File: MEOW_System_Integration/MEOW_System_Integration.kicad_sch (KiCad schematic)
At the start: 1 part

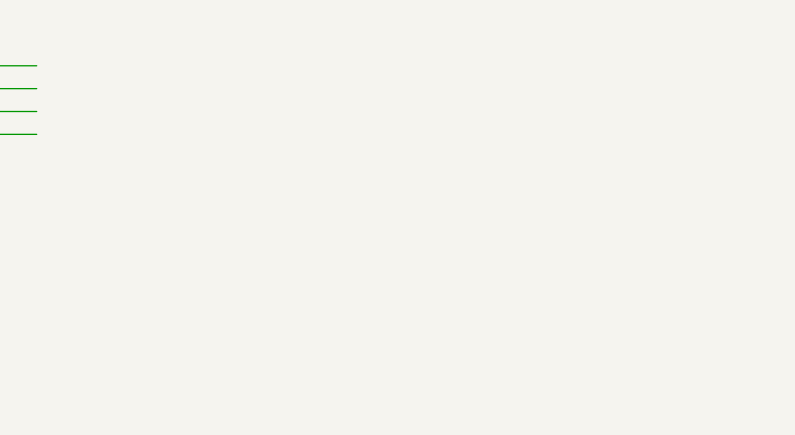
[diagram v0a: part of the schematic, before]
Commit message: Added Physical Enclsoure files
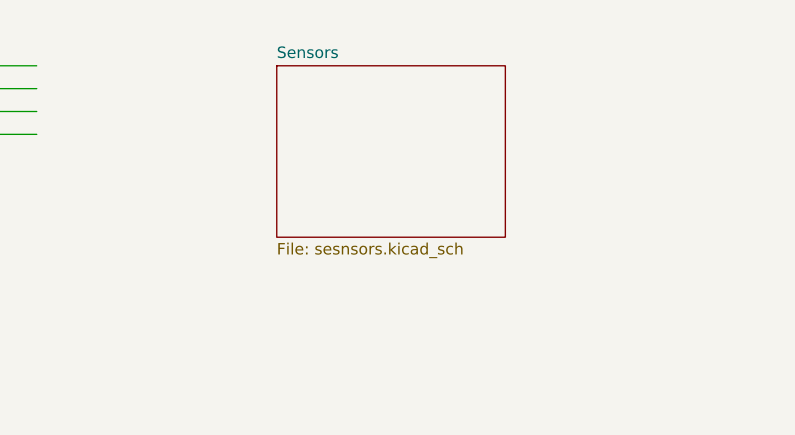
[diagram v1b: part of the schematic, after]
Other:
- added sheet Sensors (sesnsors.kicad_sch)
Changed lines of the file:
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@@
+	)
+	(sheet
+		(at 153.67 22.86)
+		(size 25.4 19.05)
+		(exclude_from_sim no)
+		(in_bom yes)
+		(on_board yes)
+		(dnp no)
+		(fields_autoplaced yes)
+		(stroke
+			(width 0.1524)
+			(type solid)
+		)
+		(fill
+			(color 0 0 0 0.0000)
+		)
+		(property "Sheetname" "Sensors"
+			(at 153.67 22.1484 0)
+			(effects
+				(font
+					(size 1.27 1.27)
+				)
+				(justify left bottom)
+			)
+		)
+		(property "Sheetfile" "sesnsors.kicad_sch"
+			(at 153.67 42.4946 0)
+			(effects
+				(font
+					(size 1.27 1.27)
+				)
+				(justify left top)
+			)
+		)
+		(instances
+			(project "MEOW_System_Integration"
+				(path "/0ce861bb-eae0-445b-b19b-9931a356f2fd"
+					(page "5")
+				)
+			)
+		)
 	)
 	(sheet

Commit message: current status PCB ordered
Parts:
- added J10, J8: Conn_01x19_Pin, Connector_PinHeader_2.54mm:PinHeader_1x19_P2.54mm_Vertical, symbol Connector:Conn_01x19_Pin
- MCU1: renamed from U3; footprint (none) -> KiCAD_Footprints:ESP32_38pin
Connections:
- net CS: now also MCU1.5 (GPIO13), J10.5 (Pin_5)
- net DIR: now also MCU1.11 (GPIO25), J10.11 (Pin_11)
- net MISO: now also MCU1.12 (GPIO32), J10.12 (Pin_12)
- net MOSI: now also MCU1.8 (GPIO14), J10.8 (Pin_8)
- net SCK: now also MCU1.9 (GPIO27), J10.9 (Pin_9)
- net STEP: now also MCU1.10 (GPIO26), J10.10 (Pin_10)
- net Vout_5V: now also MCU1.1 (5V), J10.1 (Pin_1)
- net RFDI_TX: now reaches MCU1.13 (GPIO33)
- net RFDI_TX: now also J10.13 (Pin_13)
- net RFDI_RX: now reaches MCU1.14 (GPIO35)
- net RFDI_RX: now also J10.14 (Pin_14)
- net at MCU1.15 (GPIO34): now also J10.15 (Pin_15)
- net at MCU1.16 (GIOP39): now also J10.16 (Pin_16)
- net at MCU1.17 (GIOP36): now also J10.17 (Pin_17)
- net at MCU1.18 (EN): now also J10.18 (Pin_18)
- net at MCU1.19 (3.3v): now also J10.19 (Pin_19)
- net at MCU1.2 (GPIO11): now also J10.2 (Pin_2)
- net at MCU1.20 (GPIO6): now also J8.1 (Pin_1)
- net at MCU1.21 (GPIO7): now also J8.2 (Pin_2)
- net at MCU1.22 (GPIO8): now also J8.3 (Pin_3)
- net at MCU1.23 (GPIO15): now also J8.4 (Pin_4)
- net at MCU1.24 (GPIO2): now also J8.5 (Pin_5)
- net at MCU1.25 (GPIO0): now also J8.6 (Pin_6)
- net at MCU1.26 (GPIO4): now also J8.7 (Pin_7)
- net at MCU1.27 (GPIO16): now also J8.8 (Pin_8)
- net at MCU1.28 (GPIO17): now also J8.9 (Pin_9)
- net at MCU1.29 (GPIO5): now also J8.10 (Pin_10)
- net at MCU1.3 (GPIO10): now also J10.3 (Pin_3)
- net loadcell1_data: now reaches MCU1.30 (GPIO18)
- net loadcell1_data: now also J8.11 (Pin_11)
- net loadcell1_clk: now reaches MCU1.31 (GPIO19)
- net loadcell1_clk: now also J8.12 (Pin_12)
- net at MCU1.32 (GND): now also J8.13 (Pin_13)
- net at MCU1.33 (GPIO21): now also J8.14 (Pin_14)
- net at MCU1.34 (GPIO3): now also J8.15 (Pin_15)
- net at MCU1.35 (GPIO1): now also J8.16 (Pin_16)
- net loadcell2_data: now reaches MCU1.36 (GPIO22)
- net loadcell2_data: now also J8.17 (Pin_17)
- net loadcell2_clk: now reaches MCU1.37 (GPIO23)
- net loadcell2_clk: now also J8.18 (Pin_18)
- net GND: now reaches MCU1.38 (GND)
- net GND: now also J8.19 (Pin_19)
- net at MCU1.4 (GPIO9): now also J10.4 (Pin_4)
- net at MCU1.6 (GND): now also J10.6 (Pin_6)
- net at MCU1.7 (GPIO12): now also J10.7 (Pin_7)
